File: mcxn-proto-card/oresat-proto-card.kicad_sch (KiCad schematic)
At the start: 11 parts, among them J1 J-SAMTEC-TFM-110-01-L-D-RA, J2 U.FL, J3 U.FL, J4 U.FL, J6 J-SAMTEC-TFM-120-X1-XXX-D-RA

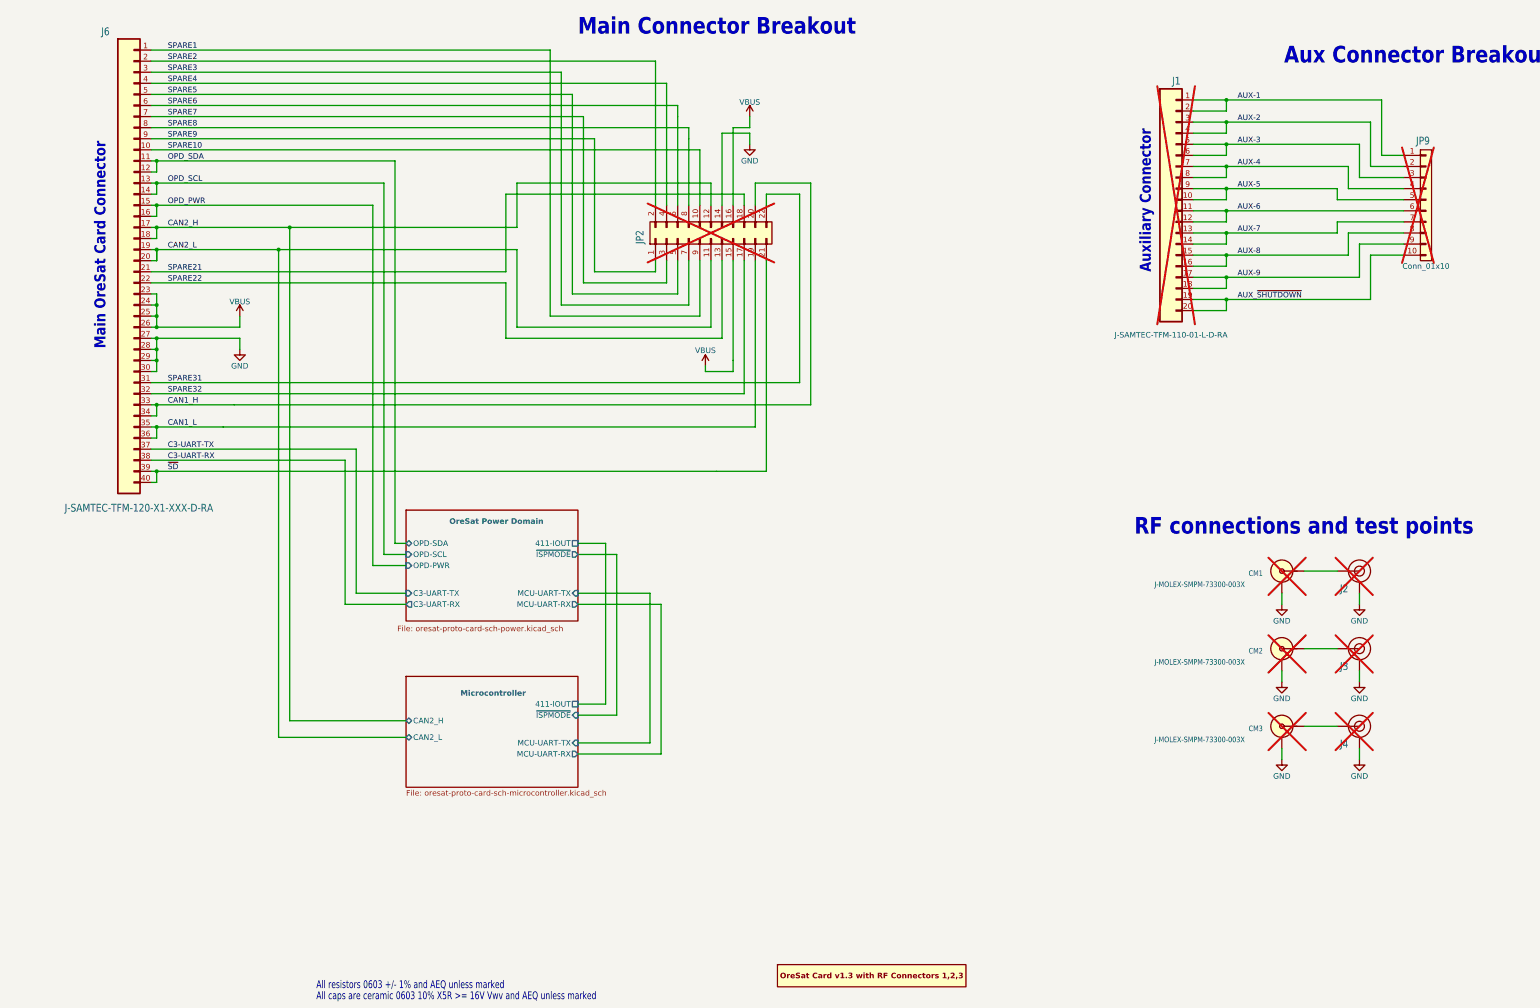
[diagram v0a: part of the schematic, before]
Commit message: Update protocard
Update to 10.0.4, new .gitignore, better hierachical layout, updated footprints, re-arranged LEDs, brought outline and SMPMs into latest standards, all but OPD is updated.
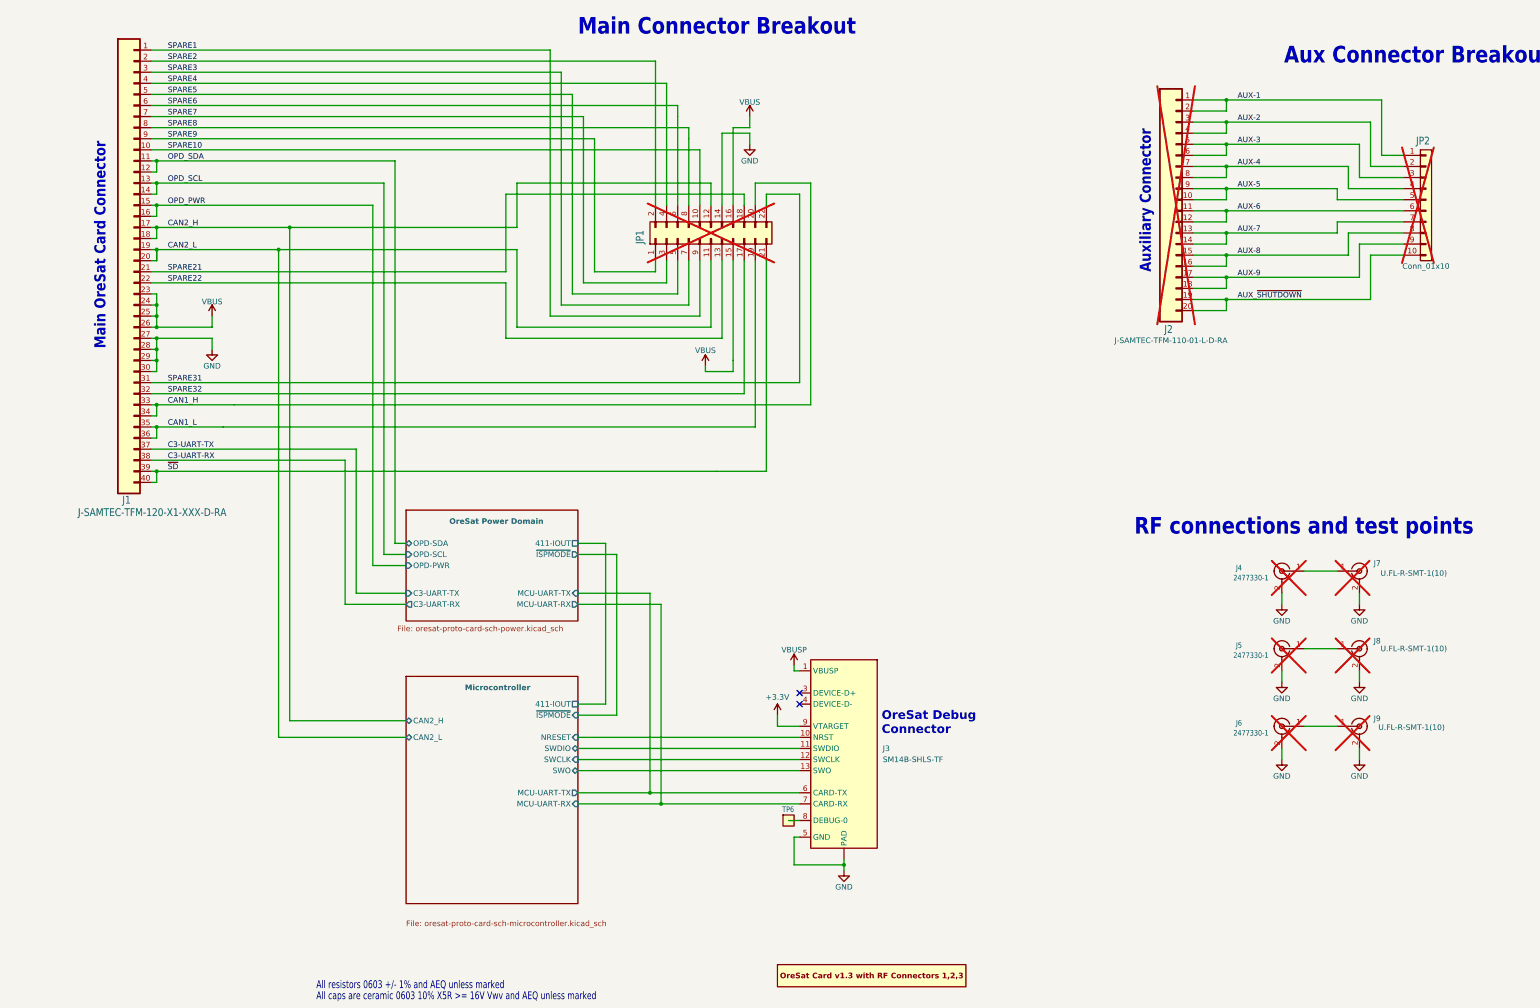
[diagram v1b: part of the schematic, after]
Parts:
- added J3: SM14B-SHLS-TF, oresat-connectors:J-JST-SM14BSHLSTF, symbol oresat-connectors:ORESAT-DEBUG-CONNECTOR-3
- added TP6: Test-Point, oresat-misc:TestPoint-0.75mm-th, symbol oresat-misc:Test-Point-0.75mm-th
- J4: renamed from CM1; value J-MOLEX-SMPM-73300-003X -> 2477330-1; symbol oresat-connectors:J-MOLEX-SMPM-73300-002X -> Connector:Conn_Coaxial; DPN WM10772-ND -> 343-2477330-1CT-ND; MFR Molex -> TE Connectivity Linx; MPN 73300-0020 -> 2477330-1
- J5: renamed from CM2; value J-MOLEX-SMPM-73300-003X -> 2477330-1; symbol oresat-connectors:J-MOLEX-SMPM-73300-002X -> Connector:Conn_Coaxial; DPN WM10772-ND -> 343-2477330-1CT-ND; MFR Molex -> TE Connectivity Linx; MPN 73300-0020 -> 2477330-1
- J6: renamed from CM3; value J-MOLEX-SMPM-73300-003X -> 2477330-1; symbol oresat-connectors:J-MOLEX-SMPM-73300-002X -> Connector:Conn_Coaxial; DPN WM10772-ND -> 343-2477330-1CT-ND; MFR Molex -> TE Connectivity Linx; MPN 73300-0020 -> 2477330-1
- J7: renamed from J2; value U.FL -> U.FL-R-SMT-1(10); footprint oresat-connectors:J-U.FL -> Connector_Coaxial:U.FL_Hirose_U.FL-R-SMT-1_Vertical; symbol oresat-connectors:U.FL2PIN -> Connector:Conn_Coaxial; DPN A118077CT-ND -> H11891CT-ND; MFR TE Connectivity -> Hirose; MPN 1909763-1 -> U.FL-R-SMT-1(10)
- J8: renamed from J3; value U.FL -> U.FL-R-SMT-1(10); footprint oresat-connectors:J-U.FL -> Connector_Coaxial:U.FL_Hirose_U.FL-R-SMT-1_Vertical; symbol oresat-connectors:U.FL2PIN -> Connector:Conn_Coaxial; DPN A118077CT-ND -> H11891CT-ND; MFR TE Connectivity -> Hirose; MPN 1909763-1 -> U.FL-R-SMT-1(10)
- J9: renamed from J4; value U.FL -> U.FL-R-SMT-1(10); footprint oresat-connectors:J-U.FL -> Connector_Coaxial:U.FL_Hirose_U.FL-R-SMT-1_Vertical; symbol oresat-connectors:U.FL2PIN -> Connector:Conn_Coaxial; DPN A118077CT-ND -> H11891CT-ND; MFR TE Connectivity -> Hirose; MPN 1909763-1 -> U.FL-R-SMT-1(10)
- renumbered J6 to J1, J1 to J2, JP2 to JP1, JP9 to JP2
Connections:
- net GND: now also J4.2 (Ext), J5.2 (Ext), J6.2 (Ext), J7.2 (Ext), J8.2 (Ext), J9.2 (Ext), J3.14 (GND), J3.15 (PAD), J3.16 (PAD), J3.5 (GND); no longer J4.SHLD, J5.SHLD, J6.SHLD, J7.GND, J8.GND, J9.GND
- net Microcontroller/MCU-UART-RX: now also J3.7 (CARD-RX)
- net Microcontroller/MCU-UART-TX: now also J3.6 (CARD-TX)
- new net: J5.1 (In), J8.1 (In)
- new net: J4.1 (In), J7.1 (In)
- new net: J3.8 (DEBUG-0), TP6.1
- new net: J6.1 (In), J9.1 (In)
- new net +3.3V: J3.9 (VTARGET)
- new net Microcontroller/NRESET: J3.10 (NRST)
- new net Microcontroller/SWCLK: J3.12 (SWCLK)
- new net Microcontroller/SWDIO: J3.11 (SWDIO)
- new net Microcontroller/SWO: J3.13 (SWO)
- new net VBUSP: J3.1 (VBUSP), J3.2 (VBUSP)
- no-connect marks 0 -> 2
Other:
- sheet Microcontroller ports: added NRESET, SWCLK, SWDIO, SWO; removed none
- note added: "OreSat Debug Connector"

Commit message: Small cleanups for manufacturing
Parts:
- added FID1, FID2, FID3: Fiducial, Fiducial:Fiducial_1mm_Mask2mm, symbol Mechanical:Fiducial
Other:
- moved on the sheet: J1, J2, J3, J4, J5, J6, J7, J8, J9, JP1, JP2, TP6
